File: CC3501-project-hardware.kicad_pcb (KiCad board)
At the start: 4 copper layers, 85 x 56 mm, 118 parts, among them J1 USB_C_Receptacle_USB2.0_16P, J2 Conn_01x03_Socket, J3 Conn_01x03_Socket, J4 Conn_01x03_Socket, J5 Conn_01x04_Socket, J6 Conn_01x08_Socket, J7 Conn_01x04, J8 Conn_01x06_Socket, J9 Conn_01x02_Socket, P2 Header 1.27mm 2x5 PTH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

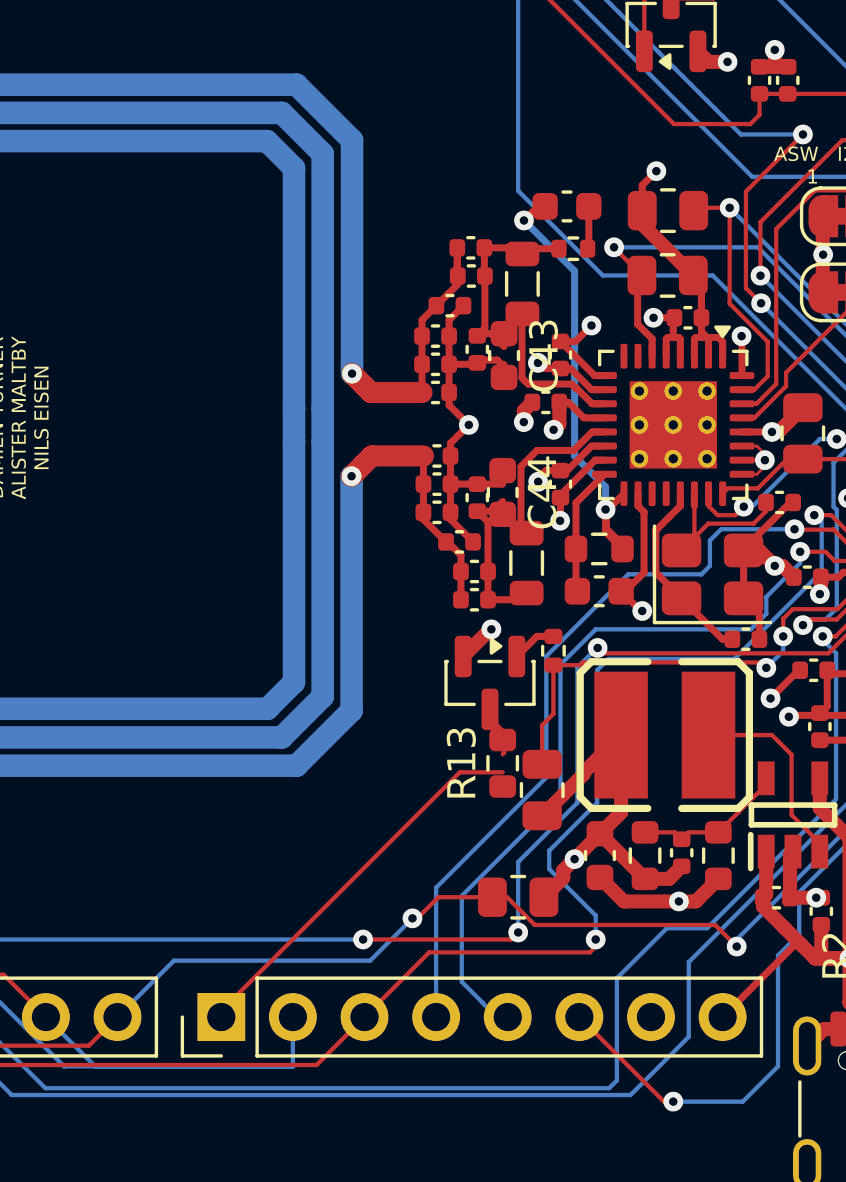
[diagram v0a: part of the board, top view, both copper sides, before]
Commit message: finished C43 and C44 and poured with b
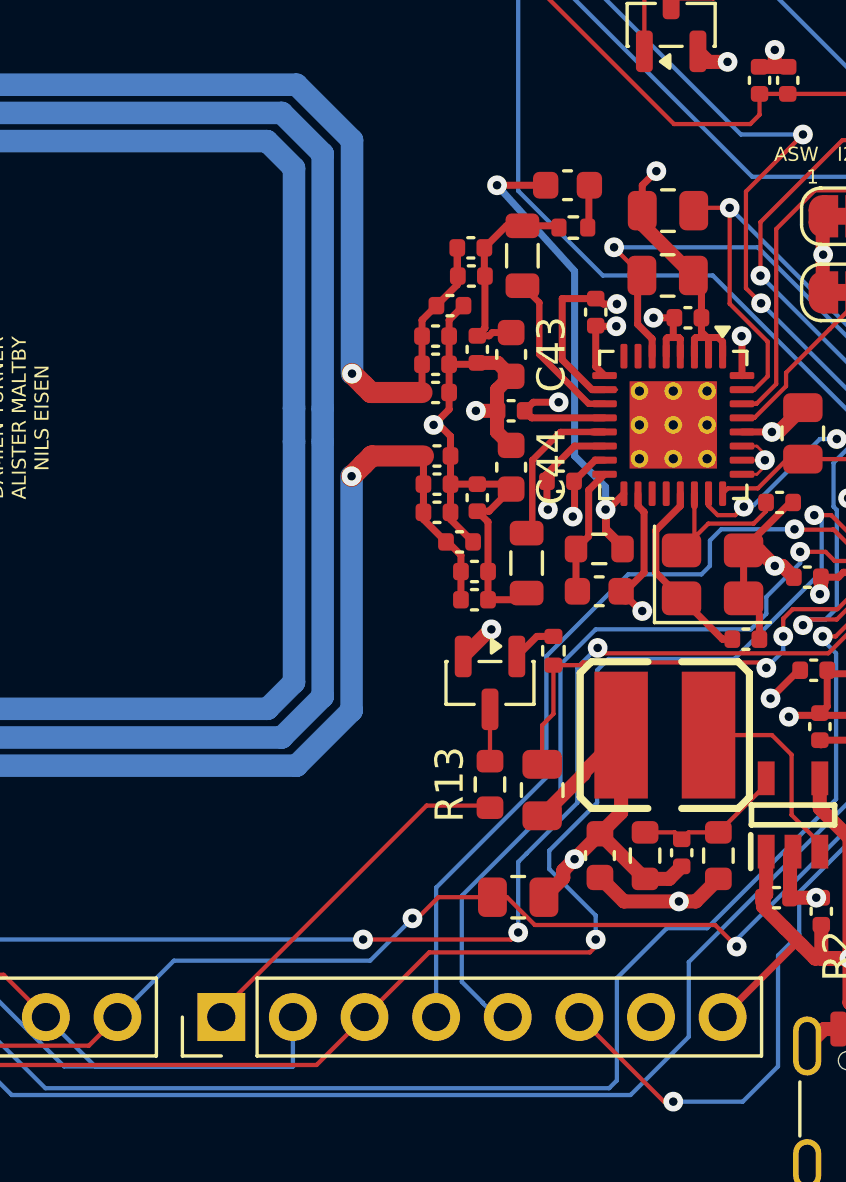
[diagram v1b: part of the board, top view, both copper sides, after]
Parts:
- moved C37 1.97 mm to (161.2, 49.0), turned to 90 degrees
- moved C35 1.27 mm to (158.2, 52.5)
- moved L3 1.00 mm to (158.7, 47.0)
- moved C44 0.94 mm to (158.2, 54.5)
- moved R13 0.87 mm to (157.5, 65.8)
- moved C34 0.75 mm to (160.2, 44.5)
- moved R24 0.75 mm to (160.5, 46.0)
- moved C43 0.25 mm to (158.2, 50.5)
- moved C36 0.10 mm to (160.0, 55.0), turned to 180 degrees
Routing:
- net GND: track 155.6 -> 160.8 mm
- net Net-(U3-RX): track 16.6 -> 19.3 mm
- net /TFT Display/LED: track 14.5 -> 13.5 mm
- net Net-(C25-Pad1): track 6.90 -> 7.53 mm

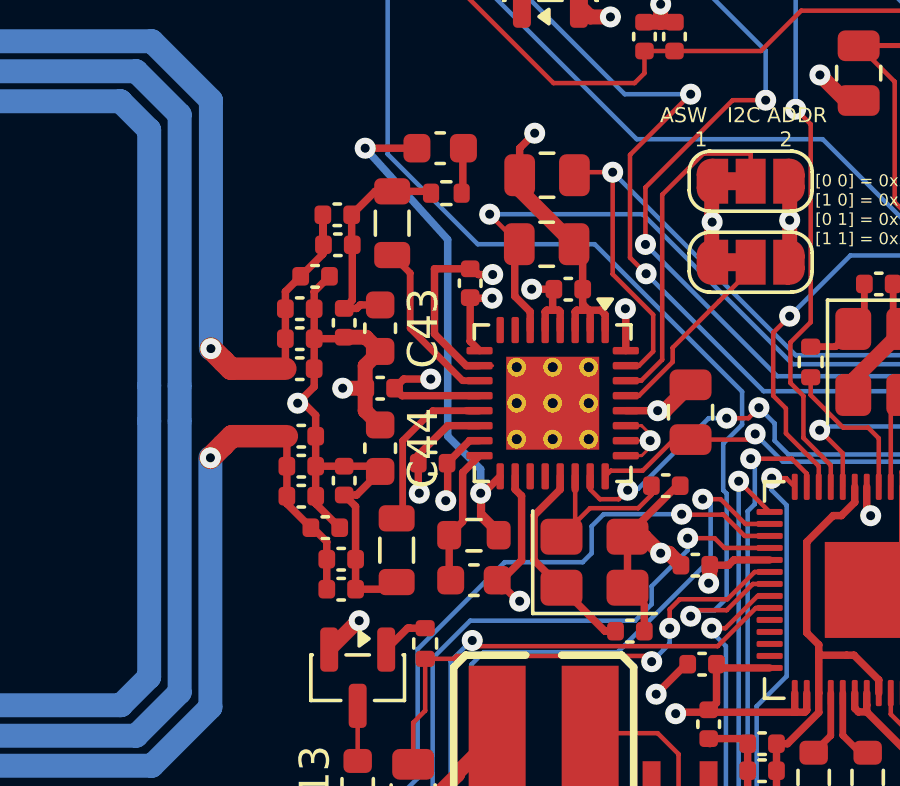
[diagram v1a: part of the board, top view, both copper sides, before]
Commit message: Fixed 3v3 gnd cap near RFID
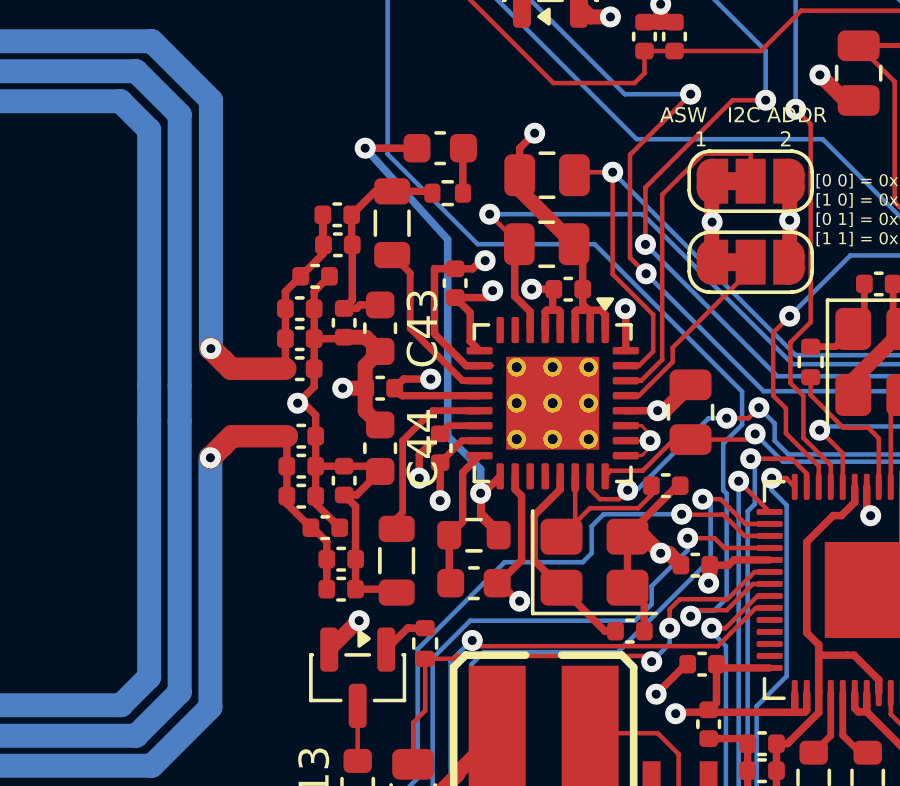
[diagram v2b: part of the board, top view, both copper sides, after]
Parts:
- moved C36 0.56 mm to (160.2, 54.5), turned to 90 degrees
- moved C37 0.50 mm to (160.8, 49.0)
- moved L2 0.35 mm to (158.8, 58.2)
- moved C33 0.10 mm to (161.4, 59.0)
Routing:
- net +3V3: track 102.4 -> 103.4 mm
- net GND: track 160.8 -> 160.0 mm
- net Net-(U3-TX2): track 5.80 -> 6.43 mm
